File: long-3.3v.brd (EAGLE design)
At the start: 20 x 50 mm, 45 parts, among them J1 CON_HEADER_1X06-SMD-RIGHT-ANG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, Q1 BSS84, U2 MCP73831, U3 MCP9808T-E/MC, X1 Micro USB, X2 CRYSTAL, X3 CRYSTALS-NOGND-IQXC-25

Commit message: Peer review complete, freeze design here!
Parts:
- added D1: POWER, SparkFun:LED-0603
- added R11: 330, SparkFun:0402-RES
- moved R10 2.21 mm to (1.20, 25.7), turned to 270 degrees
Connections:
- new net N$8: D1.A, R11.1
- new net N$9: R11.2, U$1.P$20
- net GND: now also D1.C, U$3.NC, U$3.RST
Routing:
- net N$9: track 0.00 -> 19.3 mm, vias 0 -> 1
- net GND: track 177.7 -> 182.5 mm, vias 23 -> 25
- net N$8: track 0.00 -> 1.10 mm
- net GPIO1: track 24.8 -> 25.7 mm
- net VCC: track 119.1 -> 119.7 mm

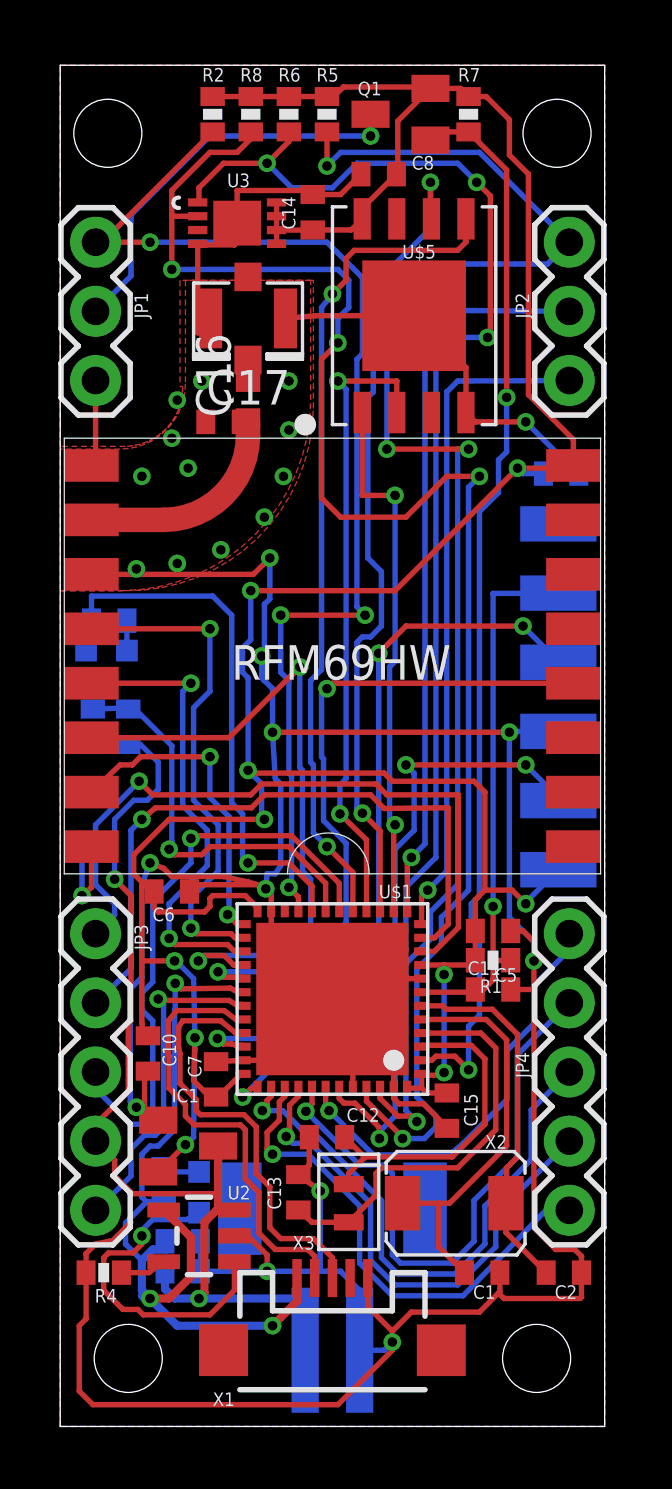
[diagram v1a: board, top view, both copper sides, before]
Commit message: Fixed Silks
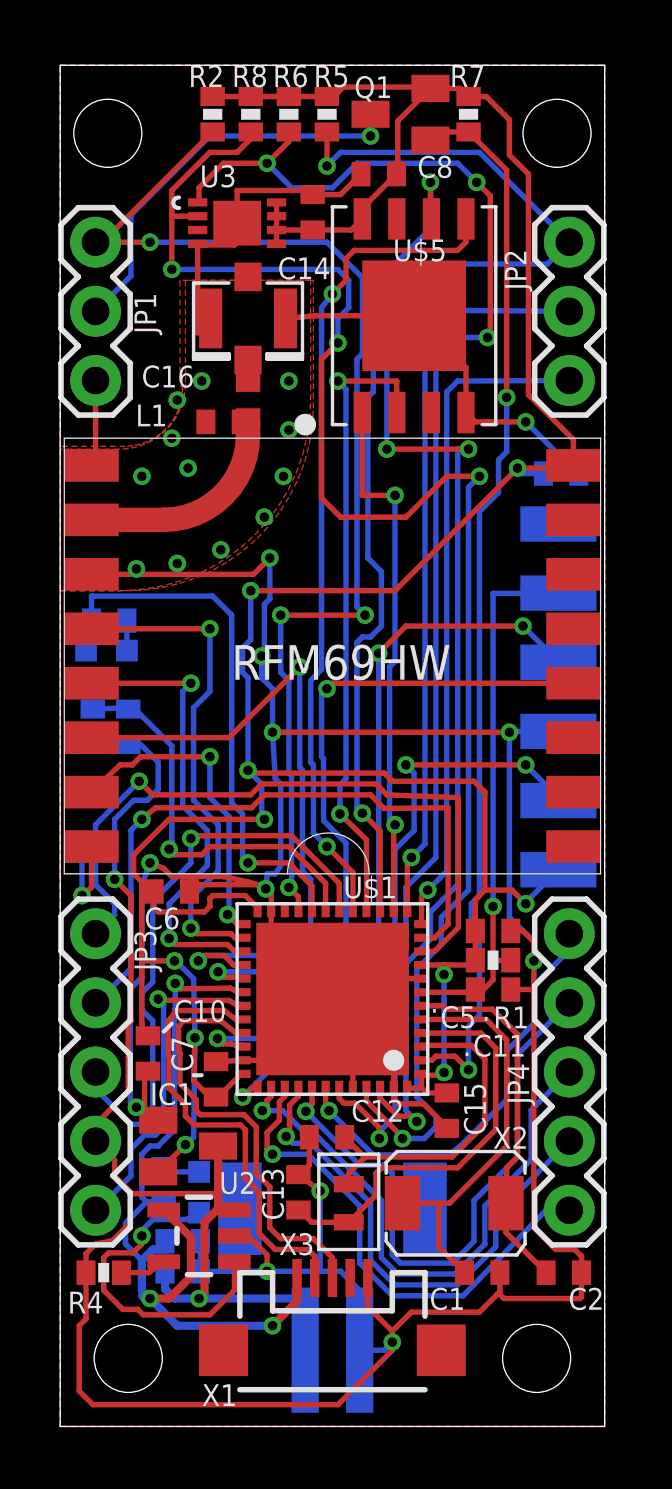
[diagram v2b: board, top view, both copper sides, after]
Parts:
- renumbered C17 to L1
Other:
- board text added: "."
- board text added: "GPSRX"
- board text added: "GPSTX"
- board text removed: "GPS_RX"
- board text removed: "GPS_TX"

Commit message: Added EARS Logo
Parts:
- added U$2: EARS-LOGO, earsLogo:EARS-LOGO
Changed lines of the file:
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@@
 <?xml version="1.0" encoding="utf-8"?>
 <!DOCTYPE eagle SYSTEM "eagle.dtd">
-<eagle version="7.3.0">
+<eagle version="7.2.0">
 <drawing>
 <settings>
@@
 <grid distance="0.1" unitdist="mm" unit="mm" style="lines" multiple="1" display="no" altdistance="0.025" altunitdist="mm" altunit="mm"/>
 <layers>
-<layer number="1" name="Top" color="4" fill="1" visible="no" active="yes"/>
-<layer number="16" name="Bottom" color="1" fill="1" visible="no" active="yes"/>
+<layer number="1" name="Top" color="4" fill="1" visible="yes" active="yes"/>
+<layer number="16" name="Bottom" color="1" fill="1" visible="yes" active="yes"/>
 <layer number="17" name="Pads" color="2" fill="1" visible="yes" active="yes"/>
 <layer number="18" name="Vias" color="2" fill="1" visible="yes" active="yes"/>
 <layer number="19" name="Unrouted" color="6" fill="1" visible="yes" active="yes"/>
 <layer number="20" name="Dimension" color="15" fill="1" visible="yes" active="yes"/>
-<layer number="21" name="tPlace" color="7" fill="1" visible="no" active="yes"/>
+<layer number="21" name="tPlace" color="7" fill="1" visible="yes" active="yes"/>
 <layer number="22" name="bPlace" color="7" fill="1" visible="yes" active="yes"/>
-<layer number="23" name="tOrigins" color="15" fill="1" visible="no" active="yes"/>
+<layer number="23" name="tOrigins" color="15" fill="1" visible="yes" active="yes"/>
 <layer number="24" name="bOrigins" color="15" fill="1" visible="yes" active="yes"/>
 <layer number="25" name="tNames" color="7" fill="1" visible="yes" active="yes"/>
@@
 <attribute name="VALUE" x="2.8795" y="28.457" size="0.8" layer="28" rot="MR0"/>
 </element>
+<element name="U$2" library="earsLogo" package="EARS-LOGO" value="EARS-LOGO" x="9.7" y="28.8" rot="MR90"/>
 </elements>
 <signals>

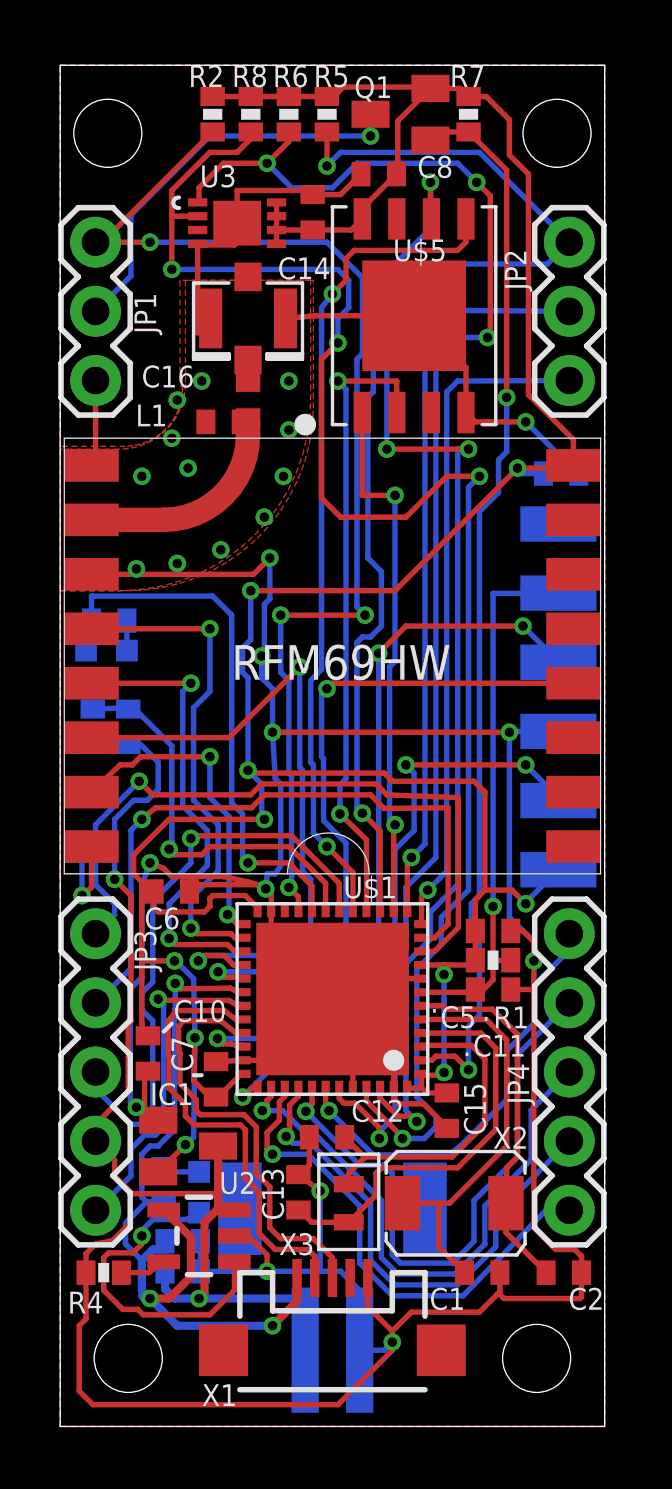
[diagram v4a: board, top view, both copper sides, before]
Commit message: Final silk check, added labels and license, shifted rf trace ground plane last time xD
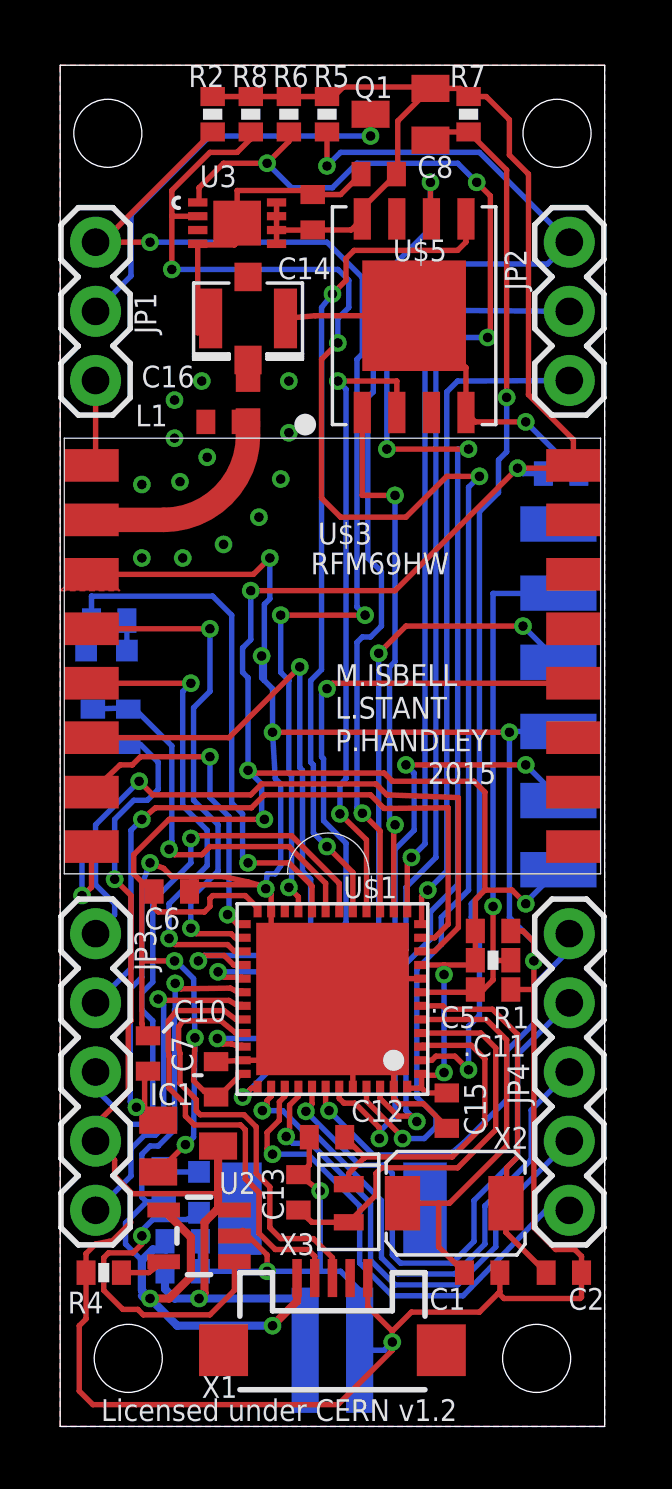
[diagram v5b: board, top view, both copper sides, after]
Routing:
- net GND: vias 25 -> 26
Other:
- board text added: "1"
- board text added: "2"
- board text added: "2015"
- board text added: "3"
- board text added: "GPIO"
- board text added: "Licensed under CERN v1.2"
- board text added: "M.ISBELL L.STANT P.HANDLEY"
- board text added: "MAIN BOARD"
- board text added: "RFM69HW"
- board text added: "SurreyEARS CTRL Board Ver 1"
- board text removed: "GPIO1"
- board text removed: "GPIO2"
- board text removed: "GPIO3"
